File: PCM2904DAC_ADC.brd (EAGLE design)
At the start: 85 x 56 mm, 48 parts, among them IC1 LM358D, Q1 12MHz, X1 V+, D-, D+, GND

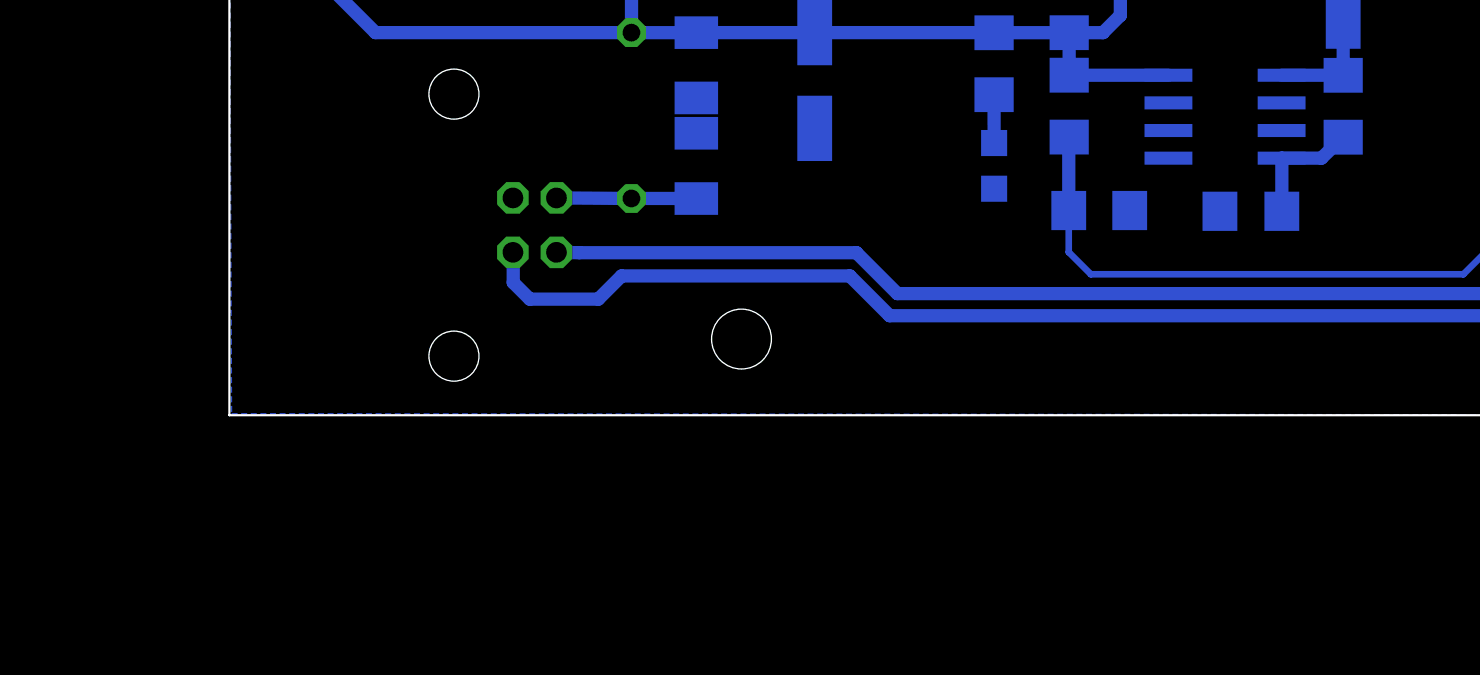
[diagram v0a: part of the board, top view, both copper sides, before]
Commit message: agregada R de 100 ohms en el sch. FALTA ACOMODARLA  EN EL PCB
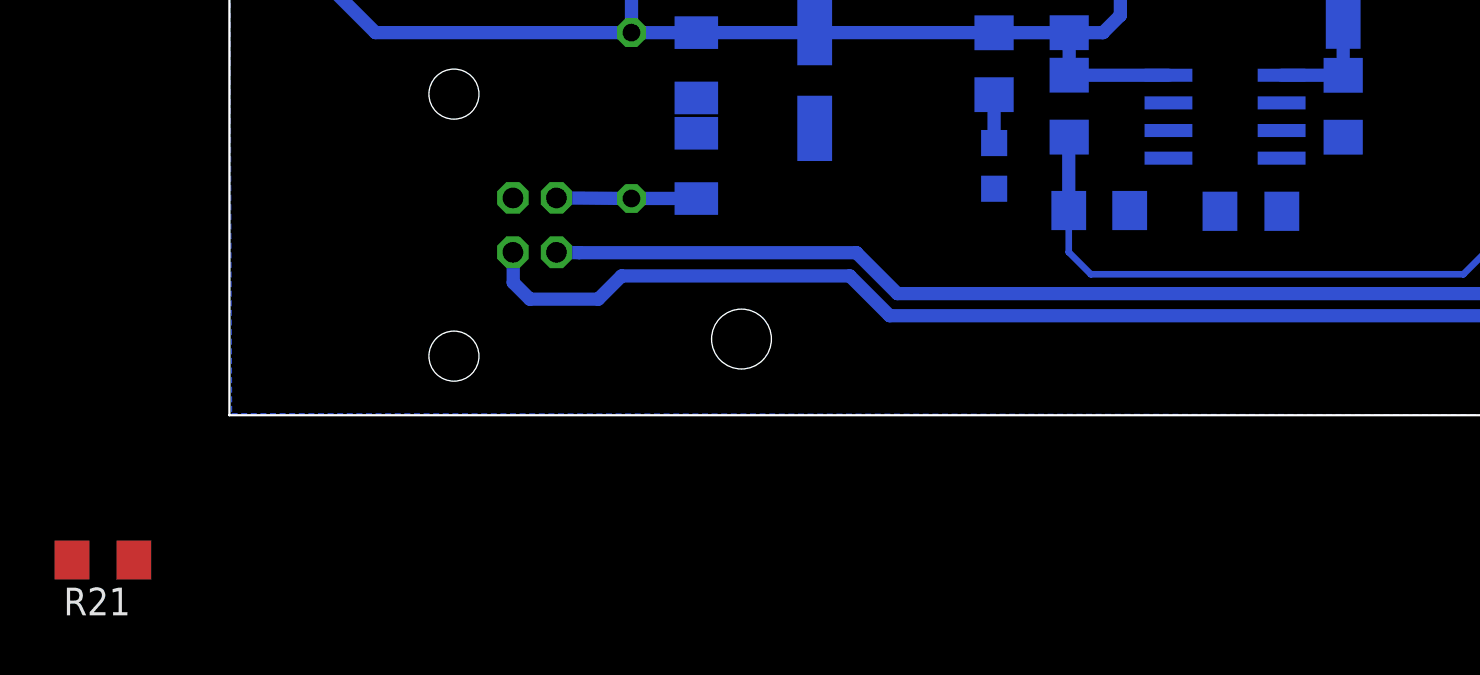
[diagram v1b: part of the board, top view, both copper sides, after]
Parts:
- added R21: 5k7, rcl:R1206
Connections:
- removed net N$41: IC2.4, R12.1, R13.1
- new net N$23: R12.1, R21.2
- new net N$26: IC2.4, R13.1, R21.1
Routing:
- net N$41: track 5.66 -> 0.00 mm
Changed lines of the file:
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@@
 <element name="U$8" library="bleep t2" package="1/8STEREO" value="1/8STEREO" x="6.5336" y="29.7688" rot="MR180"/>
 <element name="U$1" library="bleep t2" package="1/8STEREO" value="1/8STEREO" x="6.5336" y="47.244" rot="MR180"/>
+<element name="R21" library="rcl" package="R1206" value="5k7" x="-5.842" y="-6.6548" rot="R180"/>
 </elements>
 <signals>
@@
 <contactref element="LED1" pad="A"/>
 <wire x1="35.1068" y1="14.7303" x2="35.1091" y2="12.5072" width="0.6096" layer="16"/>
-</signal>
-<signal name="N$41">
-<contactref element="R12" pad="1"/>
-<contactref element="R13" pad="1"/>
-<contactref element="IC2" pad="4"/>
-<wire x1="48.3293" y1="9.3712" x2="48.3293" y2="11.8026" width="0.6096" layer="16"/>
-<wire x1="48.3293" y1="11.8026" x2="48.3194" y2="11.8125" width="0.6096" layer="16"/>
-<wire x1="48.3194" y1="11.8125" x2="50.1517" y2="11.8125" width="0.6096" layer="16"/>
-<wire x1="50.1517" y1="11.8125" x2="51.1489" y2="12.7754" width="0.6096" layer="16"/>
 </signal>
 <signal name="N$3">
@@
 <wire x1="52.9648" y1="32.7018" x2="52.9793" y2="32.7197" width="0.3048" layer="16"/>
 </signal>
+<signal name="N$23">
+<contactref element="R12" pad="1"/>
+<contactref element="R21" pad="2"/>
+<wire x1="-7.264" y1="-6.6548" x2="51.1489" y2="12.7754" width="0" layer="19" extent="1-16"/>
+</signal>
+<signal name="N$26">
+<contactref element="R13" pad="1"/>
+<contactref element="R21" pad="1"/>
+<contactref element="IC2" pad="4"/>
+<wire x1="48.3293" y1="9.3712" x2="48.3194" y2="11.8125" width="0" layer="19" extent="16-16"/>
+<wire x1="-4.42" y1="-6.6548" x2="48.3293" y2="9.3712" width="0" layer="19" extent="1-16"/>
+</signal>
 </signals>
